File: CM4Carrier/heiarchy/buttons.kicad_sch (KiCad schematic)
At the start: 9 parts

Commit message: kjkl
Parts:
- gave numbers to parts that had none: 7
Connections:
- net GLOBAL-EN: now also U2.1
- net DET_SHUTDOWN: now reaches C9.1, R5.1, R6.1, SW1.2
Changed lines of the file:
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@@
   (junction (at 62.23 146.05) (diameter 0) (color 0 0 0 0)
   )
+  (junction (at 116.84 140.97) (diameter 0) (color 0 0 0 0)
+  )
+  (junction (at 62.23 143.51) (diameter 0) (color 0 0 0 0)
+  )
+  (wire (pts (xy 116.84 140.97) (xy 119.38 140.97))
+    (stroke (width 0) (type default) (color 0 0 0 0))
+  )
   (wire (pts (xy 72.39 138.43) (xy 74.93 138.43))
     (stroke (width 0) (type default) (color 0 0 0 0))
@@
     (stroke (width 0) (type default) (color 0 0 0 0))
   )
+  (wire (pts (xy 82.55 151.13) (xy 82.55 140.97))
+    (stroke (width 0) (type default) (color 0 0 0 0))
+  )
   (wire (pts (xy 74.93 157.48) (xy 74.93 156.21))
     (stroke (width 0) (type default) (color 0 0 0 0))
   )
+  (wire (pts (xy 115.57 140.97) (xy 116.84 140.97))
+    (stroke (width 0) (type default) (color 0 0 0 0))
+  )
   (wire (pts (xy 74.93 138.43) (xy 100.33 138.43))
     (stroke (width 0) (type default) (color 0 0 0 0))
   )
+  (wire (pts (xy 82.55 140.97) (xy 85.09 140.97))
+    (stroke (width 0) (type default) (color 0 0 0 0))
+  )
   (wire (pts (xy 62.23 146.05) (xy 62.23 147.32))
     (stroke (width 0) (type default) (color 0 0 0 0))
   )
+  (wire (pts (xy 57.15 143.51) (xy 62.23 143.51))
+    (stroke (width 0) (type default) (color 0 0 0 0))
+  )
   (wire (pts (xy 62.23 157.48) (xy 62.23 160.02))
     (stroke (width 0) (type default) (color 0 0 0 0))
@@
     (stroke (width 0) (type default) (color 0 0 0 0))
   )
+  (wire (pts (xy 82.55 151.13) (xy 116.84 151.13))
+    (stroke (width 0) (type default) (color 0 0 0 0))
+  )
   (wire (pts (xy 20.32 163.83) (xy 20.32 165.1))
     (stroke (width 0) (type default) (color 0 0 0 0))
@@
     (stroke (width 0) (type default) (color 0 0 0 0))
   )
-  (wire (pts (xy 62.23 138.43) (xy 62.23 146.05))
+  (wire (pts (xy 116.84 140.97) (xy 116.84 151.13))
+    (stroke (width 0) (type default) (color 0 0 0 0))
+  )
+  (wire (pts (xy 62.23 143.51) (xy 62.23 146.05))
+    (stroke (width 0) (type default) (color 0 0 0 0))
+  )
+  (wire (pts (xy 62.23 138.43) (xy 62.23 143.51))
     (stroke (width 0) (type default) (color 0 0 0 0))
   )
@@
     (effects (font (size 1.27 1.27)) (justify right bottom))
   )
-  (hierarchical_label "GLOBAL-EN" (shape output) (at 115.57 140.97 0)
+  (hierarchical_label "DET_SHUTDOWN" (shape output) (at 57.15 143.51 180)
+    (effects (font (size 1.27 1.27)) (justify right))
+  )
+  (hierarchical_label "GLOBAL-EN" (shape output) (at 119.38 140.97 0)
     (effects (font (size 1.27 1.27)) (justify left))
   )
   (symbol (lib_id "Device:C") (at 68.58 138.43 90) (unit 1)
     (in_bom yes) (on_board yes) (fields_autoplaced)
-    (property "Reference" "C?" (id 0) (at 68.58 130.81 90))
+    (property "Reference" "C9" (id 0) (at 68.58 130.81 90))
     (property "Value" "1u" (id 1) (at 68.58 133.35 90))
     (property "Footprint" "" (id 2) (at 72.39 137.4648 0)
@@
   (symbol (lib_id "Device:R") (at 74.93 134.62 180) (unit 1)
     (in_bom yes) (on_board yes)
-    (property "Reference" "R?" (id 0) (at 77.47 133.35 0))
+    (property "Reference" "R7" (id 0) (at 77.47 133.35 0))
     (property "Value" "100k" (id 1) (at 78.74 135.89 0))
     (property "Footprint" "" (id 2) (at 76.708 134.62 90)
@@
   (symbol (lib_id "74xx:74HC00") (at 20.32 177.8 0) (unit 5)
     (in_bom yes) (on_board yes) (fields_autoplaced)
-    (property "Reference" "U?" (id 0) (at 26.67 176.5299 0)
+    (property "Reference" "U2" (id 0) (at 26.67 176.5299 0)
       (effects (font (size 1.27 1.27)) (justify left))
     )
@@
   (symbol (lib_id "power:GND") (at 20.32 190.5 0) (unit 1)
     (in_bom yes) (on_board yes) (fields_autoplaced)
-    (property "Reference" "#PWR?" (id 0) (at 20.32 196.85 0)
+    (property "Reference" "#PWR010" (id 0) (at 20.32 196.85 0)
       (effects (font (size 1.27 1.27)) hide)
     )
@@
   (symbol (lib_id "Switch:SW_Push") (at 62.23 152.4 90) (unit 1)
     (in_bom yes) (on_board yes)
-    (property "Reference" "SW?" (id 0) (at 57.15 152.4 0))
+    (property "Reference" "SW1" (id 0) (at 57.15 152.4 0))
     (property "Value" "SW_Push" (id 1) (at 64.77 152.4 0))
     (property "Footprint" "" (id 2) (at 57.15 152.4 0)
@@
   (symbol (lib_id "Device:C") (at 74.93 152.4 0) (unit 1)
     (in_bom yes) (on_board yes)
-    (property "Reference" "C?" (id 0) (at 77.47 151.13 0)
+    (property "Reference" "C10" (id 0) (at 77.47 151.13 0)
       (effects (font (size 1.27 1.27)) (justify left))
     )
@@
   (symbol (lib_id "74xx:74HC00") (at 107.95 140.97 0) (unit 2)
     (in_bom yes) (on_board yes) (fields_autoplaced)
-    (property "Reference" "U?" (id 0) (at 107.95 132.08 0))
+    (property "Reference" "U2" (id 0) (at 107.95 132.08 0))
     (property "Value" "74HC00" (id 1) (at 107.95 134.62 0))
     (property "Footprint" "" (id 2) (at 107.95 140.97 0)
@@
   (symbol (lib_id "Device:R") (at 68.58 146.05 90) (unit 1)
     (in_bom yes) (on_board yes)
-    (property "Reference" "R?" (id 0) (at 68.58 143.51 90))
+    (property "Reference" "R6" (id 0) (at 68.58 143.51 90))
     (property "Value" "5M" (id 1) (at 68.58 146.05 90))
     (property "Footprint" "" (id 2) (at 68.58 147.828 90)
@@
   (symbol (lib_id "power:GND") (at 62.23 160.02 0) (unit 1)
     (in_bom yes) (on_board yes) (fields_autoplaced)
-    (property "Reference" "#PWR?" (id 0) (at 62.23 166.37 0)
+    (property "Reference" "#PWR011" (id 0) (at 62.23 166.37 0)
       (effects (font (size 1.27 1.27)) hide)
     )
@@
   (symbol (lib_id "Device:R") (at 62.23 134.62 180) (unit 1)
     (in_bom yes) (on_board yes)
-    (property "Reference" "R?" (id 0) (at 64.77 133.35 0))
+    (property "Reference" "R5" (id 0) (at 64.77 133.35 0))
     (property "Value" "100k" (id 1) (at 66.04 135.89 0))
     (property "Footprint" "" (id 2) (at 64.008 134.62 90)
@@
   (symbol (lib_id "74xx:74HC00") (at 92.71 143.51 0) (unit 1)
     (in_bom yes) (on_board yes) (fields_autoplaced)
-    (property "Reference" "U?" (id 0) (at 92.71 134.62 0))
+    (property "Reference" "U2" (id 0) (at 92.71 134.62 0))
     (property "Value" "74HC00" (id 1) (at 92.71 137.16 0))
     (property "Footprint" "" (id 2) (at 92.71 143.51 0)

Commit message: Additions
- Fixed gitignore (Backups)
- Work on buttons
- Work on ADC for JOYSTICK
- Work on some other stuff
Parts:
- added C?: (no value), symbol Device:C
- added C? (x9): 100n, symbol Device:C
- added J?: (no value), symbol Connector:Conn_01x04_Female
- added R? (x4): (no value), symbol Device:R
- added R? (x9): 1k, symbol Device:R
- added R? (x9): 10k, symbol Device:R
- added SW?: (no value), symbol Switch:SW_Push
- added SW? (x9): SW_Push, symbol Switch:SW_Push
- added TP? (x9): ~, symbol Connector:TestPoint_Flag
- added TP?: (no value), symbol Connector:TestPoint_Flag
- added U?: (no value), symbol Analog_ADC:MCP3002
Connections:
- net GLOBAL-EN: now also R?.1, R?.2; no longer U2.1, U2.6
- net GND: now also C?.2, C?.2, C?.2, C?.2, C?.2, C?.2, C?.2, C?.2, C?.2, C?.2, J?.3 (Pin_3), R?.2, SW?.1, SW?.1, SW?.1, SW?.1, SW?.1, SW?.1, SW?.1, SW?.1, SW?.1, SW?.1, U?.4 (VSS)
- new net: R?.1, SW?.2 (x10)
- new net: R?.1, U2.1, U2.6
- new net: J?.4 (Pin_4), U?.2 (CH0)
- new net: J?.2 (Pin_2), U?.3 (CH1)
- new net A: C?.1, R?.2, R?.2, TP?.1
- new net ADC_MISO: U?.6 (DOUT)
- new net ADC_MOSI: U?.5 (DIN)
- new net ADC_SCLK: U?.7 (CLK)
- new net B: C?.1, R?.2, R?.2, TP?.1
- new net DPAD_D: C?.1, R?.2, R?.2, TP?.1
- new net DPAD_L: C?.1, R?.2, R?.2, TP?.1
- new net DPAD_R: C?.1, R?.2, R?.2, TP?.1
- new net DPAD_U: C?.1, R?.2, R?.2, TP?.1
- new net SEL: C?.1, R?.2, R?.2, TP?.1
- new net START: C?.1, R?.2, R?.2, TP?.1
- new net V_GPIO: J?.1 (Pin_1), R?.1, R?.1, R?.1, R?.1, R?.1, R?.1, R?.1, R?.1, R?.1, R?.1, U?.8 (VDD/VREF)
- new net X: C?.1, R?.2, R?.2, TP?.1
- new net Y: C?.1, R?.2, R?.2, TP?.1
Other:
- note added: "Joystick + ADC"
- note added: "Power switching circuitry should not use GPIO_VOLTAGE as when GLOBAL_EN is LOW GPIO_VOLTAGE is 0 (PMIC offline)"
- note added: "Square Pin (1) is VCC."
- moved on the sheet: C10, C9, R5, R6, R7, SW1, U2A, U2B

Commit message: wiring some stuff
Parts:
- C?: value (none) -> 100nF
- J?: value (none) -> Conn_01x04_Female
- R?: value (none) -> 1k
- R? (x2): value (none) -> 10k
- R?: value (none) -> 2K7
- SW?: value (none) -> SW_Push
- TP?: value (none) -> TestPoint_Flag
- U?: value (none) -> MCP3002
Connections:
- net ADC_CS': now reaches U?.1 (~{CS}/SHDN)
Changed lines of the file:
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@@
+    (stroke (width 0) (type default) (color 0 0 0 0))
+  )
+  (wire (pts (xy 261.62 124.46) (xy 262.89 124.46))
     (stroke (width 0) (type default) (color 0 0 0 0))
   )
@@
     (effects (font (size 1.27 1.27)) (justify left))
   )
+  (hierarchical_label "ADC_CS'" (shape input) (at 262.89 124.46 0)
+    (effects (font (size 1.27 1.27)) (justify left))
+  )
   (hierarchical_label "SEL" (shape output) (at 66.04 128.27 0)
     (effects (font (size 1.27 1.27)) (justify left))
   )
-  (hierarchical_label "ADC_MOSI" (shape output) (at 262.89 134.62 0)
+  (hierarchical_label "ADC_MOSI" (shape input) (at 262.89 134.62 0)
     (effects (font (size 1.27 1.27)) (justify left))
   )
@@
     (in_bom yes) (on_board yes) (fields_autoplaced)
     (property "Reference" "R?" (id 0) (at 198.12 39.37 90))
-    (property "Value" "" (id 1) (at 198.12 41.91 90))
+    (property "Value" "1k" (id 1) (at 198.12 41.91 90))
     (property "Footprint" "" (id 2) (at 198.12 47.498 90)
       (effects (font (size 1.27 1.27)) hide)
@@
       (effects (font (size 1.27 1.27)) (justify right))
     )
-    (property "Value" "" (id 1) (at 193.04 54.6099 90)
+    (property "Value" "SW_Push" (id 1) (at 193.04 54.6099 90)
       (effects (font (size 1.27 1.27)) (justify right))
     )
@@
       (effects (font (size 1.27 1.27)) (justify left))
     )
-    (property "Value" "" (id 1) (at 208.28 55.8799 0)
+    (property "Value" "100nF" (id 1) (at 208.28 55.8799 0)
       (effects (font (size 1.27 1.27)) (justify left))
     )
@@
       (effects (font (size 1.27 1.27)) (justify left))
     )
-    (property "Value" "" (id 1) (at 219.71 46.8629 0)
+    (property "Value" "TestPoint_Flag" (id 1) (at 219.71 46.8629 0)
       (effects (font (size 1.27 1.27)) (justify left) hide)
     )
@@
       (effects (font (size 1.27 1.27)) hide)
     )
-    (property "Value" "" (id 1) (at 189.23 64.77 0))
+    (property "Value" "GND" (id 1) (at 189.23 64.77 0))
     (property "Footprint" "" (id 2) (at 189.23 59.69 0)
       (effects (font (size 1.27 1.27)) hide)
@@
       (effects (font (size 1.27 1.27)) (justify left))
     )
-    (property "Value" "" (id 1) (at 207.01 41.9099 0)
+    (property "Value" "10k" (id 1) (at 207.01 41.9099 0)
       (effects (font (size 1.27 1.27)) (justify left))
     )
@@
       (effects (font (size 1.27 1.27)) (justify left))
     )
-    (property "Value" "" (id 1) (at 130.81 177.7999 0)
+    (property "Value" "10k" (id 1) (at 130.81 177.7999 0)
       (effects (font (size 1.27 1.27)) (justify left))
     )
@@
       (effects (font (size 1.27 1.27)) (justify left))
     )
-    (property "Value" "" (id 1) (at 245.8594 116.84 0)
+    (property "Value" "MCP3002" (id 1) (at 245.8594 116.84 0)
       (effects (font (size 1.27 1.27)) (justify left))
     )
@@
       (effects (font (size 1.27 1.27)) hide)
     )
-    (property "Value" "" (id 1) (at 128.27 186.69 0))
+    (property "Value" "GND" (id 1) (at 128.27 186.69 0))
     (property "Footprint" "" (id 2) (at 128.27 181.61 0)
       (effects (font (size 1.27 1.27)) hide)
@@
       (effects (font (size 1.27 1.27)) hide)
     )
-    (property "Value" "" (id 1) (at 224.79 149.86 0))
+    (property "Value" "GND" (id 1) (at 224.79 149.86 0))
     (property "Footprint" "" (id 2) (at 224.79 144.78 0)
       (effects (font (size 1.27 1.27)) hide)
@@
     (in_bom yes) (on_board yes) (fields_autoplaced)
     (property "Reference" "J?" (id 0) (at 203.835 124.46 0))
-    (property "Value" "" (id 1) (at 203.835 127 0))
+    (property "Value" "Conn_01x04_Female" (id 1) (at 203.835 127 0))
     (property "Footprint" "" (id 2) (at 203.2 134.62 0)
       (effects (font (size 1.27 1.27)) hide)
@@
     (in_bom yes) (on_board yes) (fields_autoplaced)
     (property "Reference" "R?" (id 0) (at 123.19 165.1 90))
-    (property "Value" "" (id 1) (at 123.19 167.64 90))
+    (property "Value" "2K7" (id 1) (at 123.19 167.64 90))
     (property "Footprint" "" (id 2) (at 123.19 173.228 90)
       (effects (font (size 1.27 1.27)) hide)

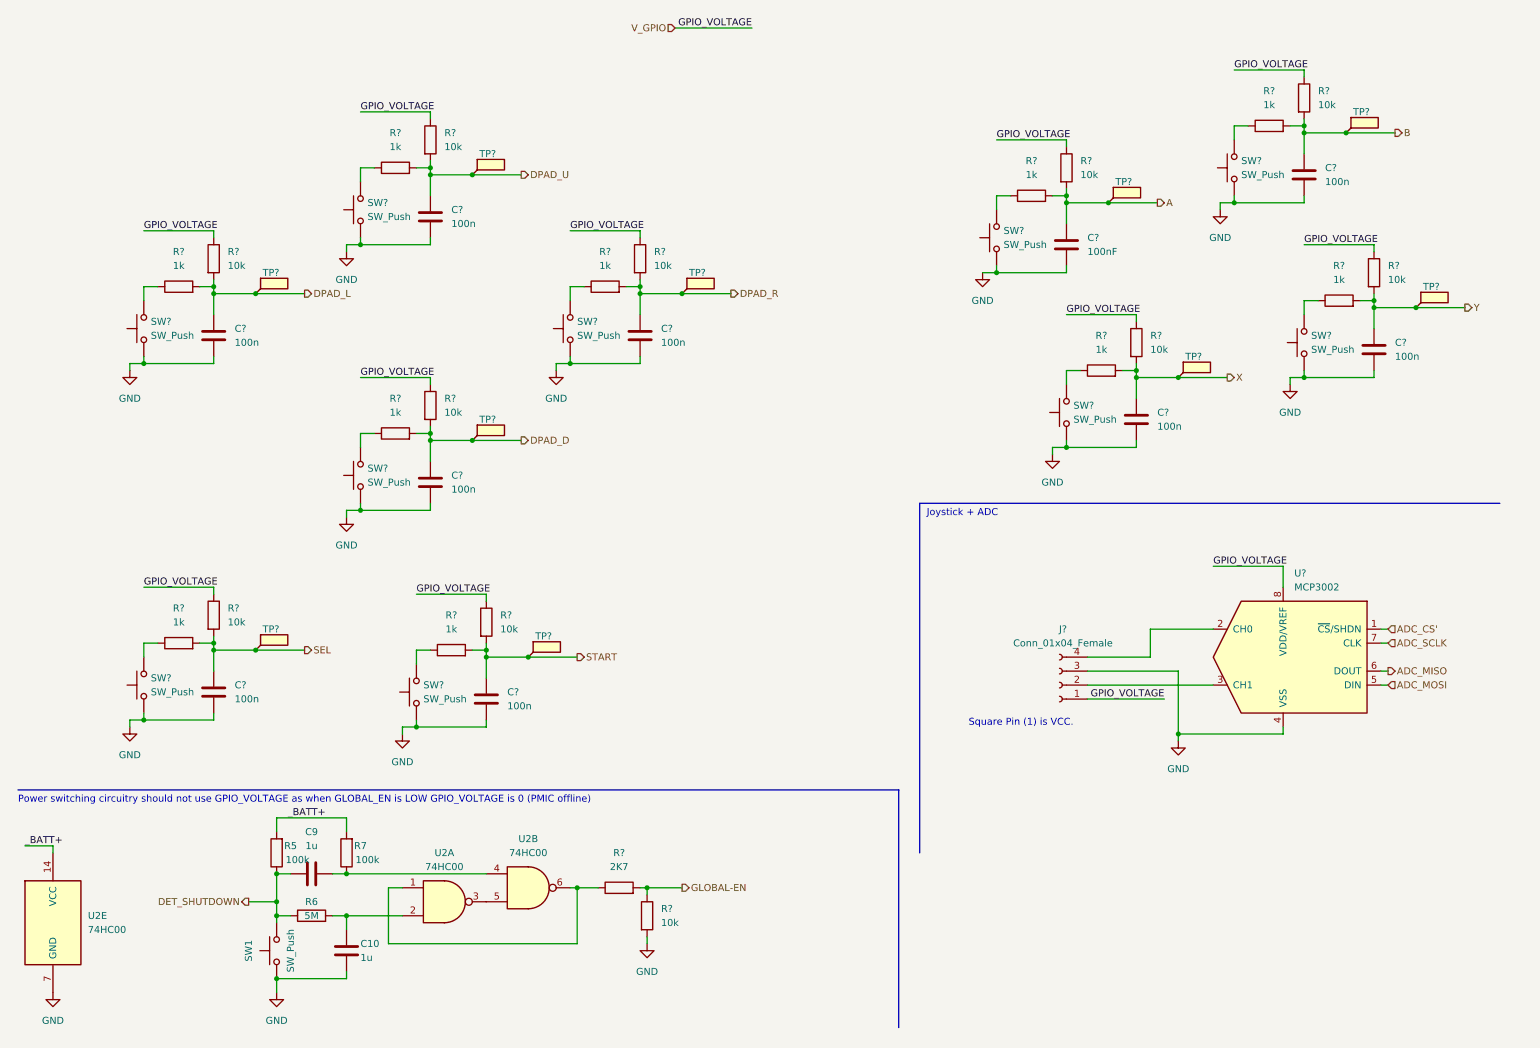
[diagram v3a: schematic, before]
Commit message: footprints  + values
need to do some 3d babeeeeeeeeee
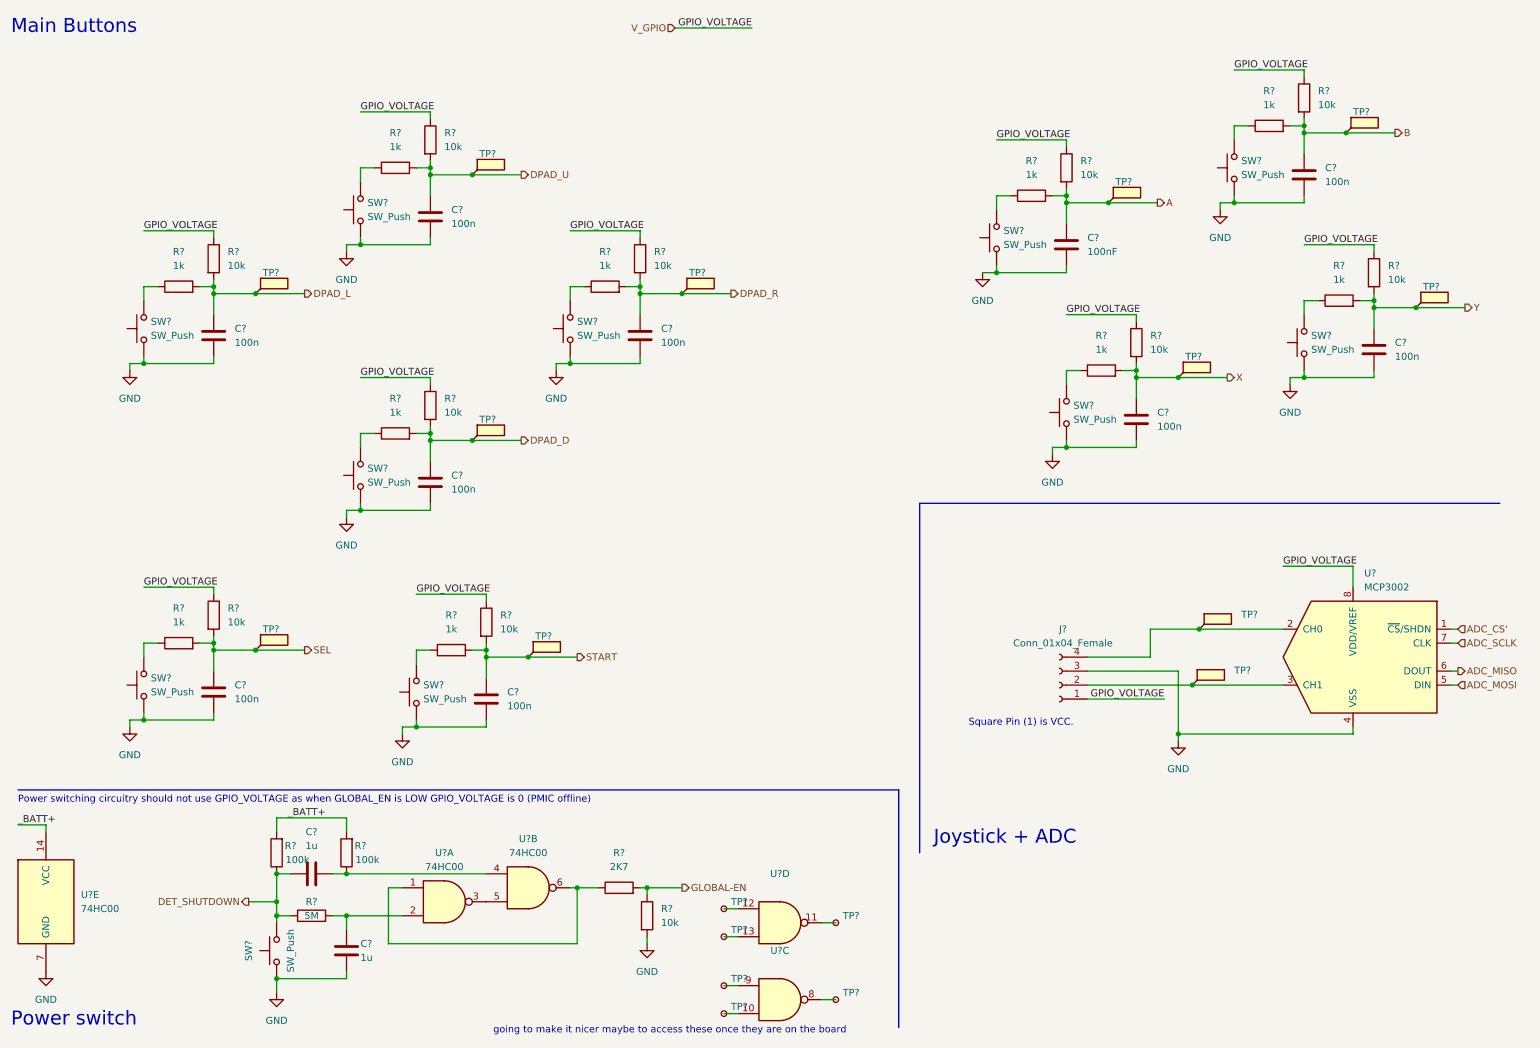
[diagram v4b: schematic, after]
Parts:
- added TP? (x6): (no value), symbol Connector:TestPoint_Small
- added TP? (x2): (no value), symbol Connector:TestPoint_Flag
- added U? (x2): (no value), symbol 74xx:74HC00
- TP? (x9): value ~ -> (none)
- TP?: value TestPoint_Flag -> (none)
- renumbered C9 to C?, C10 to C?, R7 to R?, R6 to R?, R5 to R?, SW1 to SW?, U2 to U?
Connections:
- net at J?.4 (Pin_4), U?.2 (CH0): now also TP?.1
- net at J?.2 (Pin_2), U?.3 (CH1): now also TP?.1
- new net: TP?.1, U?.9
- new net: TP?.1, U?.11
- new net: TP?.1, U?.13
- new net: TP?.1, U?.10
- new net: TP?.1, U?.8
- new net: TP?.1, U?.12
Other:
- note added: "Main Buttons"
- note added: "Power switch"
- note added: "going to make it nicer maybe to access these once they are on the board"
- moved on the sheet: U?, U?E
